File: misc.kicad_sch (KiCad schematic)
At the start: 23 parts, among them J6 Conn_ARM_JTAG_SWD_10, SW1 SW_DIP_x02, U1 MIMX8MM6DVTLZAA, Y4 24Mhz

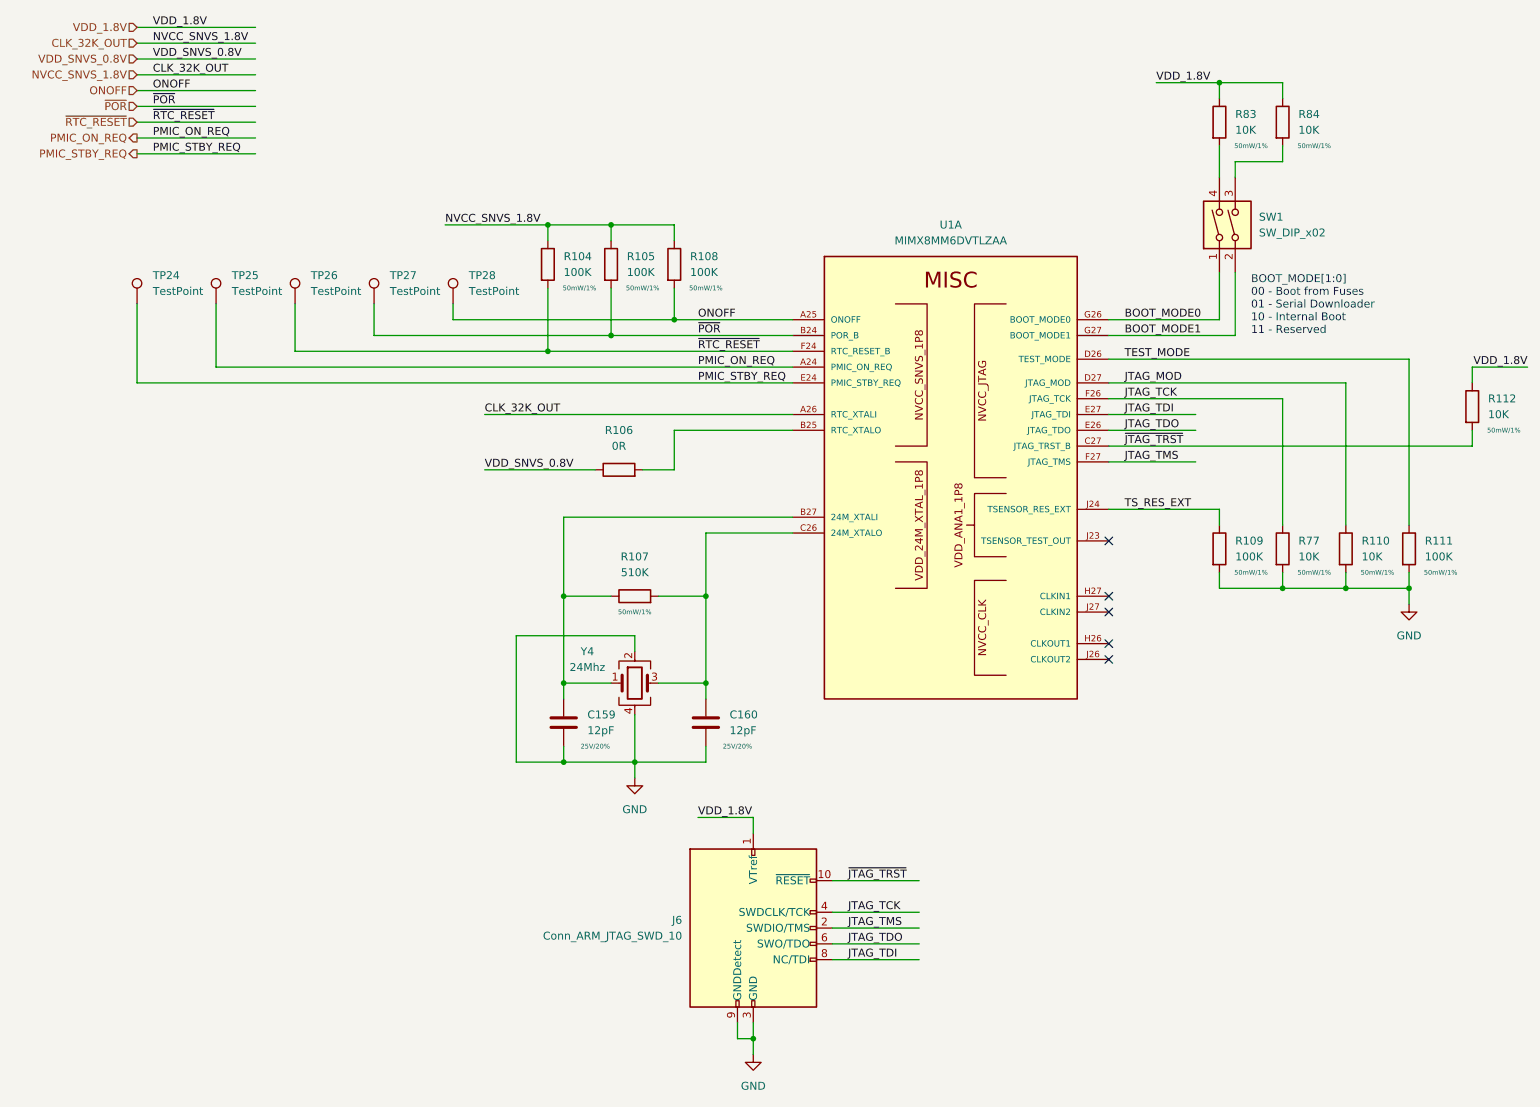
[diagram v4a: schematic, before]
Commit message: fix ref desgigators, add table for dram config
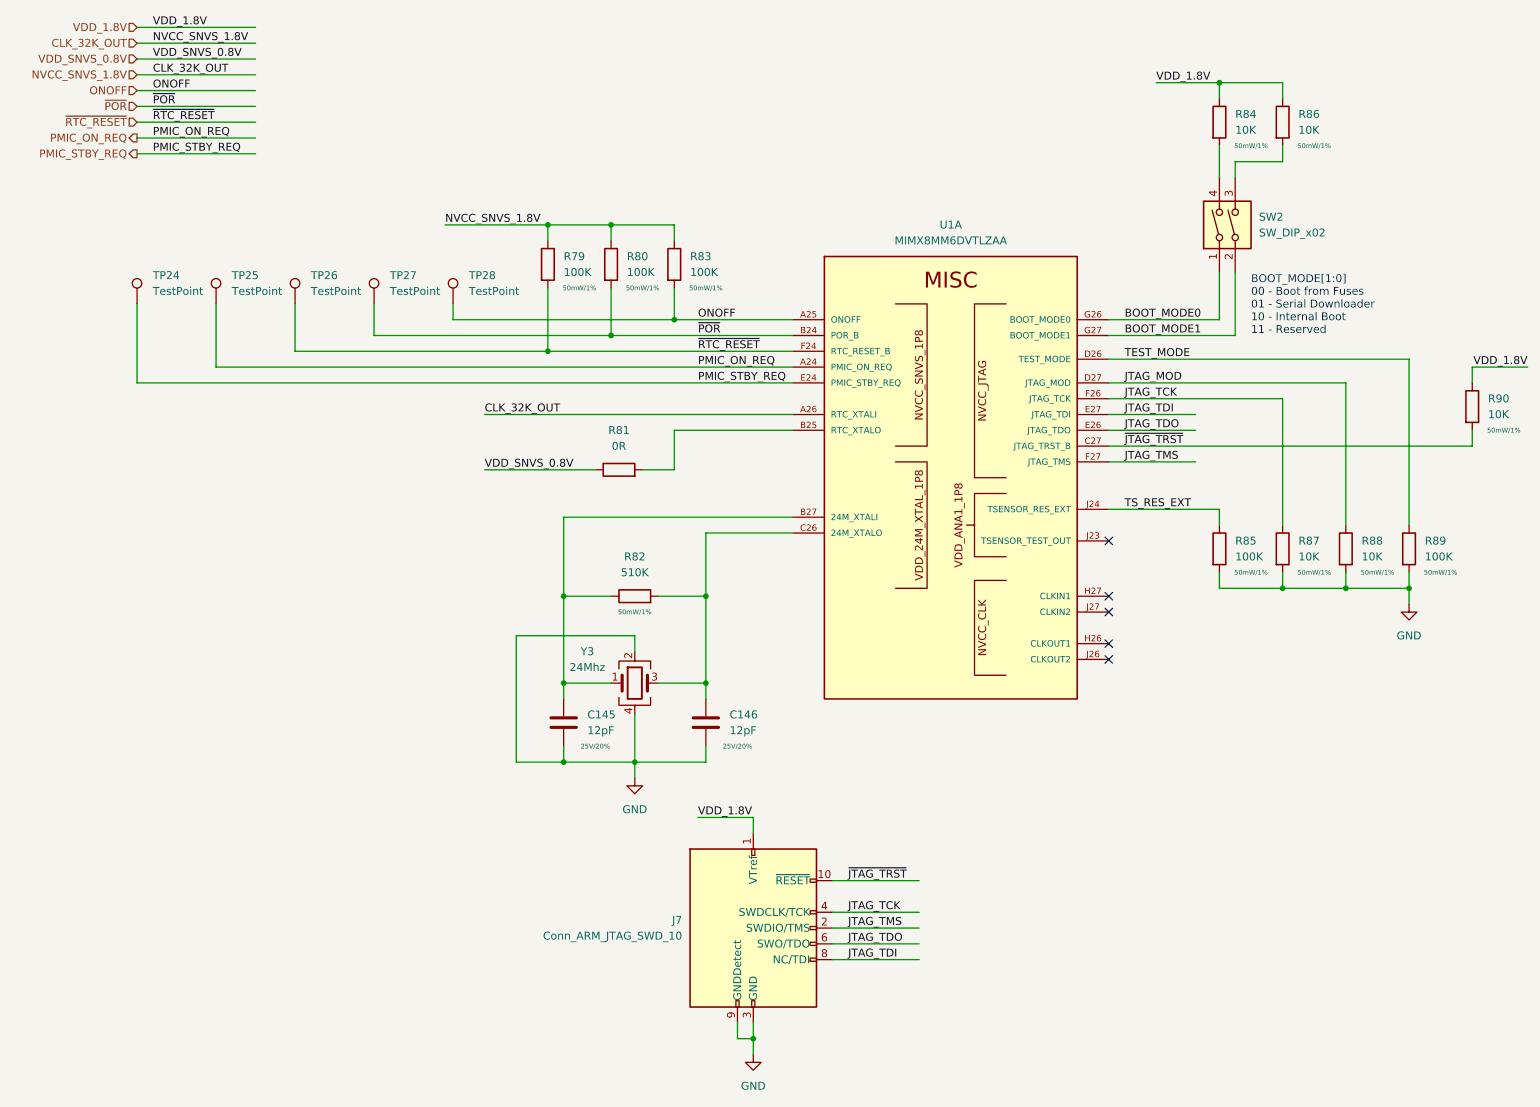
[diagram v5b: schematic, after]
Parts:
- renumbered C159 to C145, C160 to C146, J6 to J7, R104 to R79, R105 to R80, R106 to R81, R107 to R82, R108 to R83, R83 to R84, R109 to R85, R84 to R86, R77 to R87, R110 to R88, R111 to R89, R112 to R90, SW1 to SW2, Y4 to Y3
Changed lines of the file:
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@@
   (symbol (lib_id "Device:C") (at 99.06 132.08 0) (unit 1)
     (in_bom yes) (on_board yes)
-    (property "Reference" "C159" (id 0) (at 102.87 130.8099 0)
+    (property "Reference" "C145" (id 0) (at 102.87 130.8099 0)
       (effects (font (size 1.27 1.27)) (justify left))
     )
@@
   (symbol (lib_id "Device:R") (at 224.79 104.14 0) (unit 1)
     (in_bom yes) (on_board yes)
-    (property "Reference" "R110" (id 0) (at 227.33 102.8699 0)
+    (property "Reference" "R88" (id 0) (at 227.33 102.8699 0)
       (effects (font (size 1.27 1.27)) (justify left))
     )
@@
   (symbol (lib_id "power:GND") (at 129.54 185.42 0) (unit 1)
     (in_bom yes) (on_board yes) (fields_autoplaced)
-    (property "Reference" "#PWR0225" (id 0) (at 129.54 191.77 0)
+    (property "Reference" "#PWR0134" (id 0) (at 129.54 191.77 0)
       (effects (font (size 1.27 1.27)) hide)
     )
@@
   (symbol (lib_id "Device:R") (at 214.63 35.56 0) (unit 1)
     (in_bom yes) (on_board yes)
-    (property "Reference" "R84" (id 0) (at 217.17 34.2899 0)
+    (property "Reference" "R86" (id 0) (at 217.17 34.2899 0)
       (effects (font (size 1.27 1.27)) (justify left))
     )
@@
   (symbol (lib_id "Device:R") (at 204.47 35.56 0) (unit 1)
     (in_bom yes) (on_board yes)
-    (property "Reference" "R83" (id 0) (at 207.01 34.2899 0)
+    (property "Reference" "R84" (id 0) (at 207.01 34.2899 0)
       (effects (font (size 1.27 1.27)) (justify left))
     )
@@
   (symbol (lib_id "Device:R") (at 96.52 58.42 0) (unit 1)
     (in_bom yes) (on_board yes)
-    (property "Reference" "R104" (id 0) (at 99.06 57.1499 0)
+    (property "Reference" "R79" (id 0) (at 99.06 57.1499 0)
       (effects (font (size 1.27 1.27)) (justify left))
     )
@@
   (symbol (lib_id "Device:R") (at 110.49 111.76 90) (unit 1)
     (in_bom yes) (on_board yes)
-    (property "Reference" "R107" (id 0) (at 110.49 105.41 90))
+    (property "Reference" "R82" (id 0) (at 110.49 105.41 90))
     (property "Value" "510K" (id 1) (at 110.49 107.95 90))
     (property "Footprint" "Resistor_SMD:R_0402_1005Metric" (id 2) (at 110.49 113.538 90)
@@
   (symbol (lib_id "power:GND") (at 110.49 140.97 0) (unit 1)
     (in_bom yes) (on_board yes) (fields_autoplaced)
-    (property "Reference" "#PWR0245" (id 0) (at 110.49 147.32 0)
+    (property "Reference" "#PWR0133" (id 0) (at 110.49 147.32 0)
       (effects (font (size 1.27 1.27)) hide)
     )
@@
   (symbol (lib_id "Device:R") (at 234.95 104.14 0) (unit 1)
     (in_bom yes) (on_board yes)
-    (property "Reference" "R111" (id 0) (at 237.49 102.8699 0)
+    (property "Reference" "R89" (id 0) (at 237.49 102.8699 0)
       (effects (font (size 1.27 1.27)) (justify left))
     )
@@
   (symbol (lib_id "Device:R") (at 214.63 104.14 0) (unit 1)
     (in_bom yes) (on_board yes)
-    (property "Reference" "R77" (id 0) (at 217.17 102.8699 0)
+    (property "Reference" "R87" (id 0) (at 217.17 102.8699 0)
       (effects (font (size 1.27 1.27)) (justify left))
     )
@@
   (symbol (lib_id "Device:R") (at 116.84 58.42 0) (unit 1)
     (in_bom yes) (on_board yes)
-    (property "Reference" "R108" (id 0) (at 119.38 57.1499 0)
+    (property "Reference" "R83" (id 0) (at 119.38 57.1499 0)
       (effects (font (size 1.27 1.27)) (justify left))
     )
@@
   (symbol (lib_id "power:GND") (at 234.95 113.03 0) (unit 1)
     (in_bom yes) (on_board yes) (fields_autoplaced)
-    (property "Reference" "#PWR0224" (id 0) (at 234.95 119.38 0)
+    (property "Reference" "#PWR0135" (id 0) (at 234.95 119.38 0)
       (effects (font (size 1.27 1.27)) hide)
     )
@@
   (symbol (lib_id "Device:R") (at 204.47 104.14 0) (unit 1)
     (in_bom yes) (on_board yes)
-    (property "Reference" "R109" (id 0) (at 207.01 102.8699 0)
+    (property "Reference" "R85" (id 0) (at 207.01 102.8699 0)
       (effects (font (size 1.27 1.27)) (justify left))
     )
@@
   (symbol (lib_id "Device:C") (at 121.92 132.08 0) (unit 1)
     (in_bom yes) (on_board yes)
-    (property "Reference" "C160" (id 0) (at 125.73 130.8099 0)
+    (property "Reference" "C146" (id 0) (at 125.73 130.8099 0)
       (effects (font (size 1.27 1.27)) (justify left))
     )
@@
   (symbol (lib_id "Device:R") (at 245.11 81.28 0) (unit 1)
     (in_bom yes) (on_board yes)
-    (property "Reference" "R112" (id 0) (at 247.65 80.0099 0)
+    (property "Reference" "R90" (id 0) (at 247.65 80.0099 0)
       (effects (font (size 1.27 1.27)) (justify left))
     )
@@
   (symbol (lib_id "Device:R") (at 106.68 58.42 0) (unit 1)
     (in_bom yes) (on_board yes)
-    (property "Reference" "R105" (id 0) (at 109.22 57.1499 0)
+    (property "Reference" "R80" (id 0) (at 109.22 57.1499 0)
       (effects (font (size 1.27 1.27)) (justify left))
     )
@@
   (symbol (lib_id "Switch:SW_DIP_x02") (at 207.01 52.07 90) (unit 1)
     (in_bom yes) (on_board yes) (fields_autoplaced)
-    (property "Reference" "SW1" (id 0) (at 210.82 50.7999 90)
+    (property "Reference" "SW2" (id 0) (at 210.82 50.7999 90)
       (effects (font (size 1.27 1.27)) (justify right))
     )
@@
   (symbol (lib_id "Device:R") (at 107.95 91.44 90) (unit 1)
     (in_bom yes) (on_board yes) (fields_autoplaced)
-    (property "Reference" "R106" (id 0) (at 107.95 85.09 90))
+    (property "Reference" "R81" (id 0) (at 107.95 85.09 90))
     (property "Value" "0R" (id 1) (at 107.95 87.63 90))
     (property "Footprint" "Resistor_SMD:R_0402_1005Metric" (id 2) (at 107.95 93.218 90)
@@
   (symbol (lib_id "Device:Crystal_GND24") (at 110.49 125.73 0) (unit 1)
     (in_bom yes) (on_board yes)
-    (property "Reference" "Y4" (id 0) (at 102.87 120.65 0))
+    (property "Reference" "Y3" (id 0) (at 102.87 120.65 0))
     (property "Value" "24Mhz" (id 1) (at 102.87 123.19 0))
     (property "Footprint" "Crystal:Crystal_SMD_3225-4Pin_3.2x2.5mm" (id 2) (at 110.49 125.73 0)
@@
   (symbol (lib_id "Connector:Conn_ARM_JTAG_SWD_10") (at 129.54 165.1 0) (unit 1)
     (in_bom yes) (on_board yes) (fields_autoplaced)
-    (property "Reference" "J6" (id 0) (at 118.11 163.8299 0)
+    (property "Reference" "J7" (id 0) (at 118.11 163.8299 0)
       (effects (font (size 1.27 1.27)) (justify right))
     )
